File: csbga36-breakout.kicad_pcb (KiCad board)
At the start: 2 copper layers, 17.8 x 48.3 mm, 3 parts, among them J1 Conn_01x18_Male, J2 Conn_01x18_Male

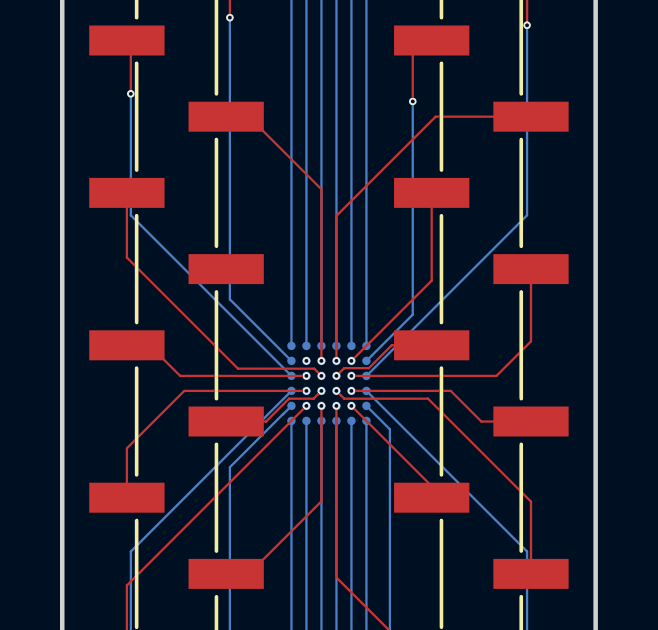
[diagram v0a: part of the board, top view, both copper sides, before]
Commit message: naming all nets, adding informational text
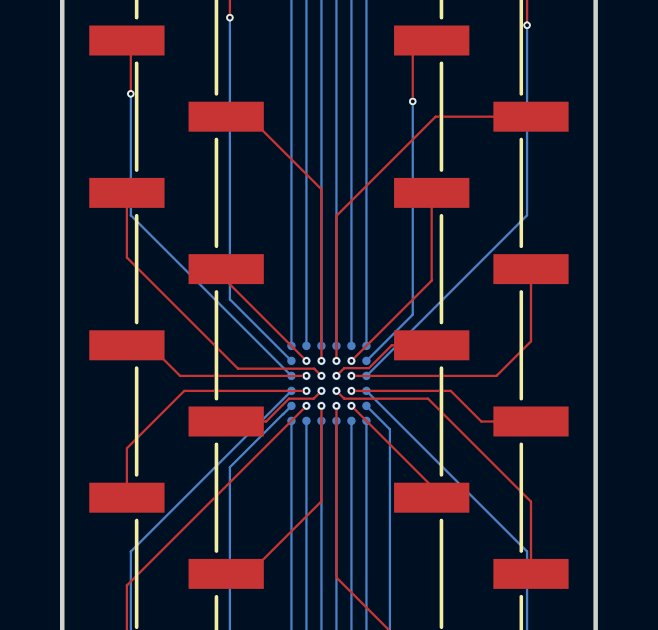
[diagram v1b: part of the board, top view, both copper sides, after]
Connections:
- net Net-(J1-Pad1) renamed /A3
- net Net-(J1-Pad10) renamed /D2
- net Net-(J1-Pad11) renamed /E2
- net Net-(J1-Pad12) renamed /D3
- net Net-(J1-Pad13) renamed /E3
- net Net-(J1-Pad14) renamed /D1
- net Net-(J1-Pad15) renamed /E1
- net Net-(J1-Pad16) renamed /F1
- net Net-(J1-Pad17) renamed /F2
- net Net-(J1-Pad18) renamed /F3
- net Net-(J1-Pad2) renamed /A2
- net Net-(J1-Pad3) renamed /A1
- net Net-(J1-Pad4) renamed /C1
- net Net-(J1-Pad5) renamed /B1
- net Net-(J1-Pad6) renamed /B3
- net Net-(J1-Pad7) renamed /B2
- net Net-(J1-Pad8) renamed /C2
- net Net-(J1-Pad9) renamed /C3
- net Net-(J2-Pad1) renamed /A4
- net Net-(J2-Pad10) renamed /D4
- net Net-(J2-Pad11) renamed /D5
- net Net-(J2-Pad12) renamed /E4
- net Net-(J2-Pad13) renamed /E5
- net Net-(J2-Pad14) renamed /E6
- net Net-(J2-Pad15) renamed /D6
- net Net-(J2-Pad16) renamed /F6
- net Net-(J2-Pad17) renamed /F5
- net Net-(J2-Pad18) renamed /F4
- net Net-(J2-Pad2) renamed /A5
- net Net-(J2-Pad3) renamed /A6
- net Net-(J2-Pad4) renamed /B6
- net Net-(J2-Pad5) renamed /C6
- net Net-(J2-Pad6) renamed /B4
- net Net-(J2-Pad7) renamed /C4
- net Net-(J2-Pad8) renamed /B5
- net Net-(J2-Pad9) renamed /C5
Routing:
- net /B5: track 0.00 -> 4.17 mm
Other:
- board text added: "6x6 BGA 0.5mm pitch"
- board text added: "A1"
- board text added: "A2"
- board text added: "A3"
- board text added: "A4"
- board text added: "A5"
- board text added: "A6"
- board text added: "B1"
- board text added: "B2"
- board text added: "B3"
- board text added: "B4"
- board text added: "B5"
- board text added: "B6"
- board text added: "C1"
- board text added: "C2"
- board text added: "C3"
- board text added: "C4"
- board text added: "C5"
- board text added: "C6"
- board text added: "D1"
- board text added: "D2"
- board text added: "D3"
- board text added: "D4"
- board text added: "D5"
- board text added: "D6"
- board text added: "E1"
- board text added: "E2"
- board text added: "E3"
- board text added: "E4"
- board text added: "E5"
- board text added: "E6"
- board text added: "F1"
- board text added: "F2"
- board text added: "F3"
- board text added: "F4"
- board text added: "F5"
- board text added: "F6"
- board text added: "tindie.com/stores/tpimh"

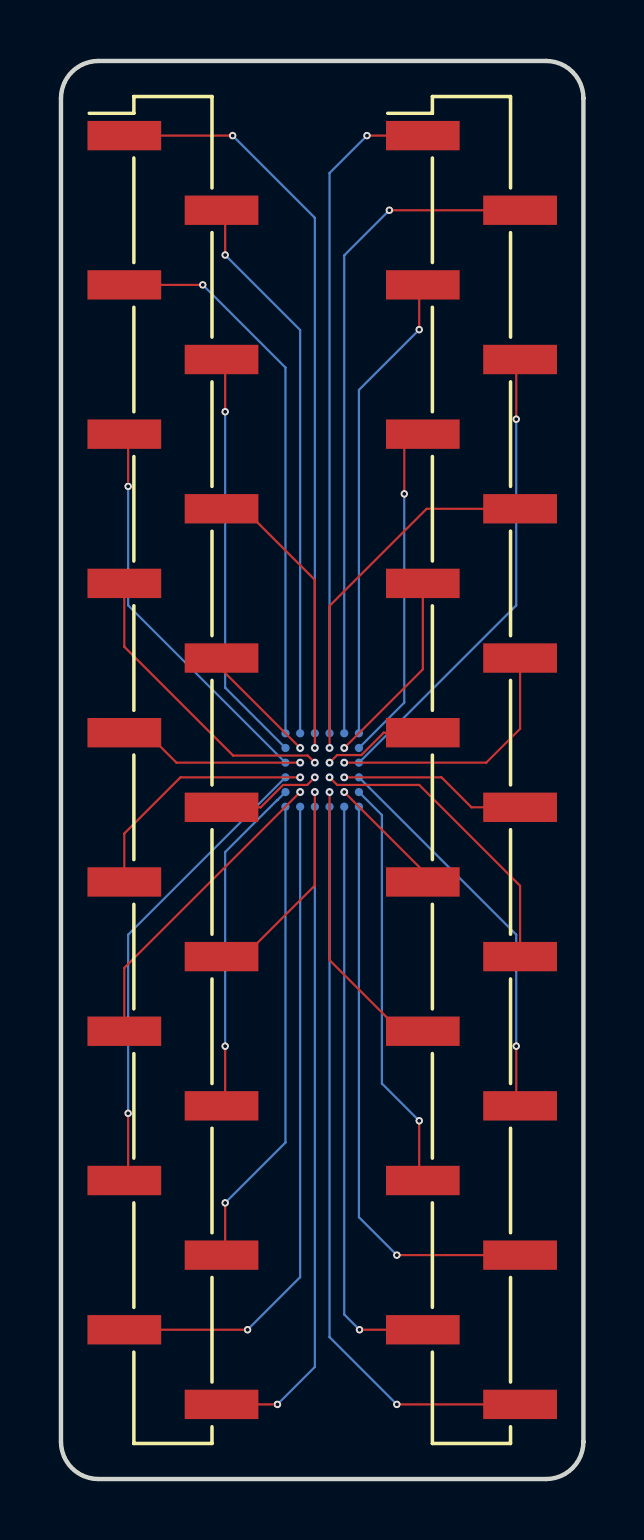
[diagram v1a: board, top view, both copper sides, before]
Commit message: move vias away from bga pads
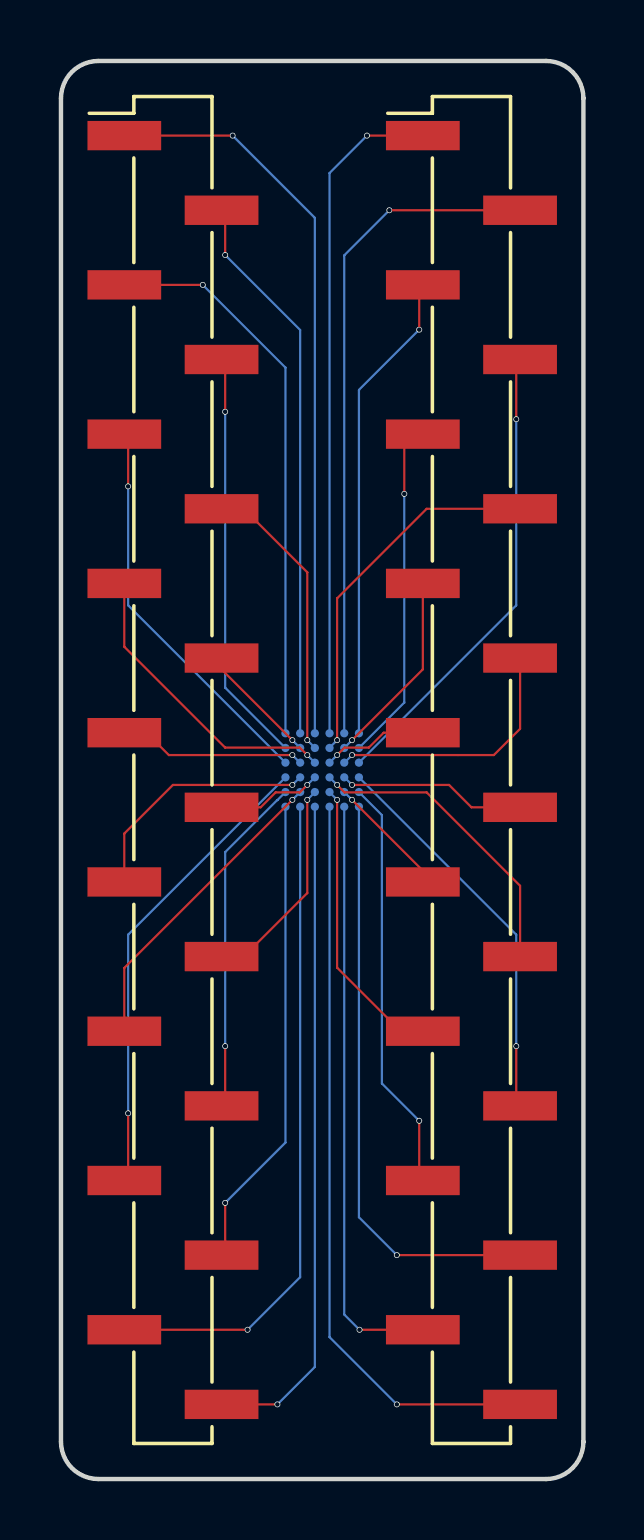
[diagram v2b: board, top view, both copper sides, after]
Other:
- net class Default: via_dia 0.254 -> 0.2; via_drill 0.127 -> 0.15
- rule via_min_drill: 0.127 -> 0.15
- rule via_min_size: 0.254 -> 0.2
